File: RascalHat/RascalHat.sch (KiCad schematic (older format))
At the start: 26 parts, among them J10 Conn_01x04_Male, J11 Conn_01x03_Male, J12 Conn_01x03_Male, J13 Conn_01x07_Male, J17 Conn_01x02_Male, J2 Conn_01x09_Male, J3 Conn_01x04_Male, J4 Conn_01x08_Male, J5 Conn_01x08_Male

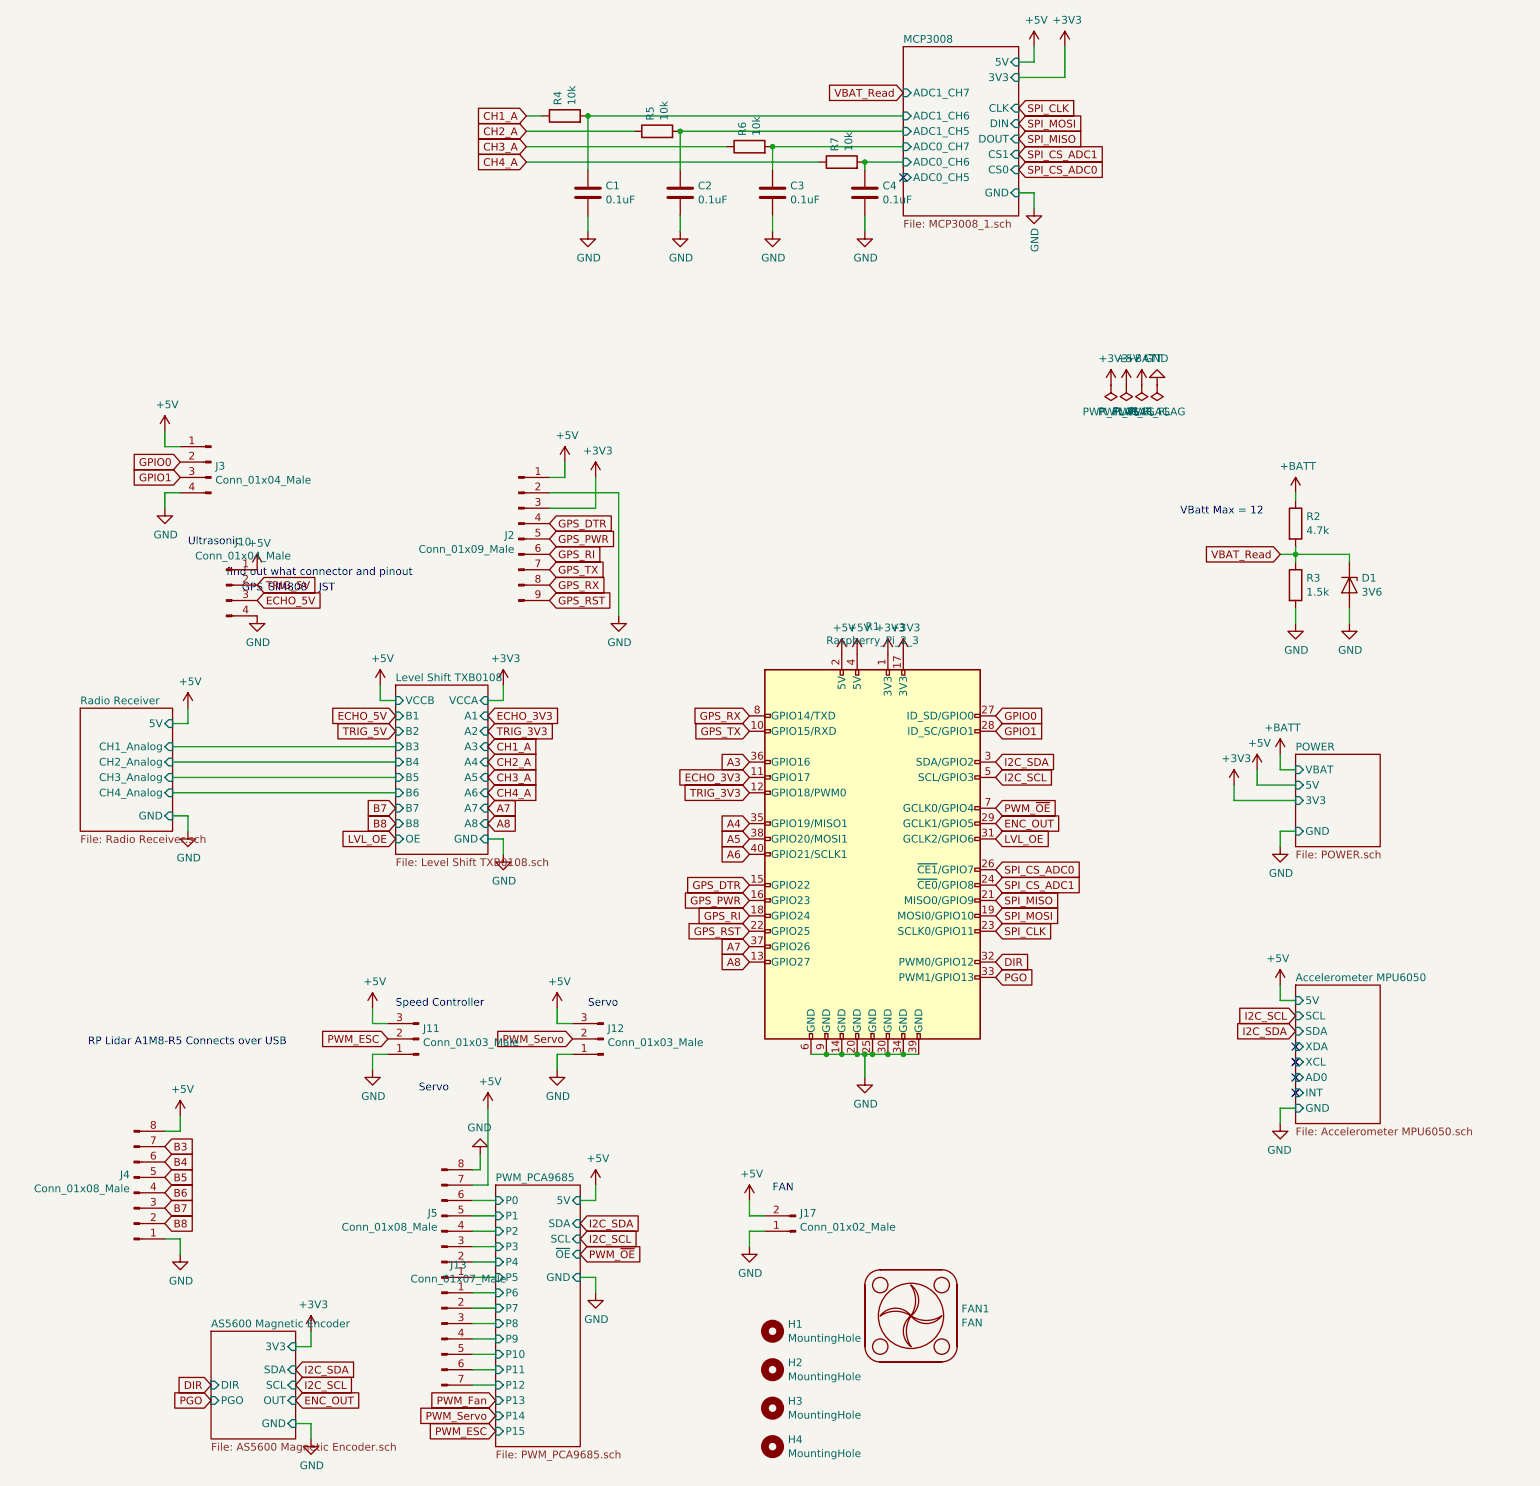
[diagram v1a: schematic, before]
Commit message: schematic updated, all footprints created, pcb layout started
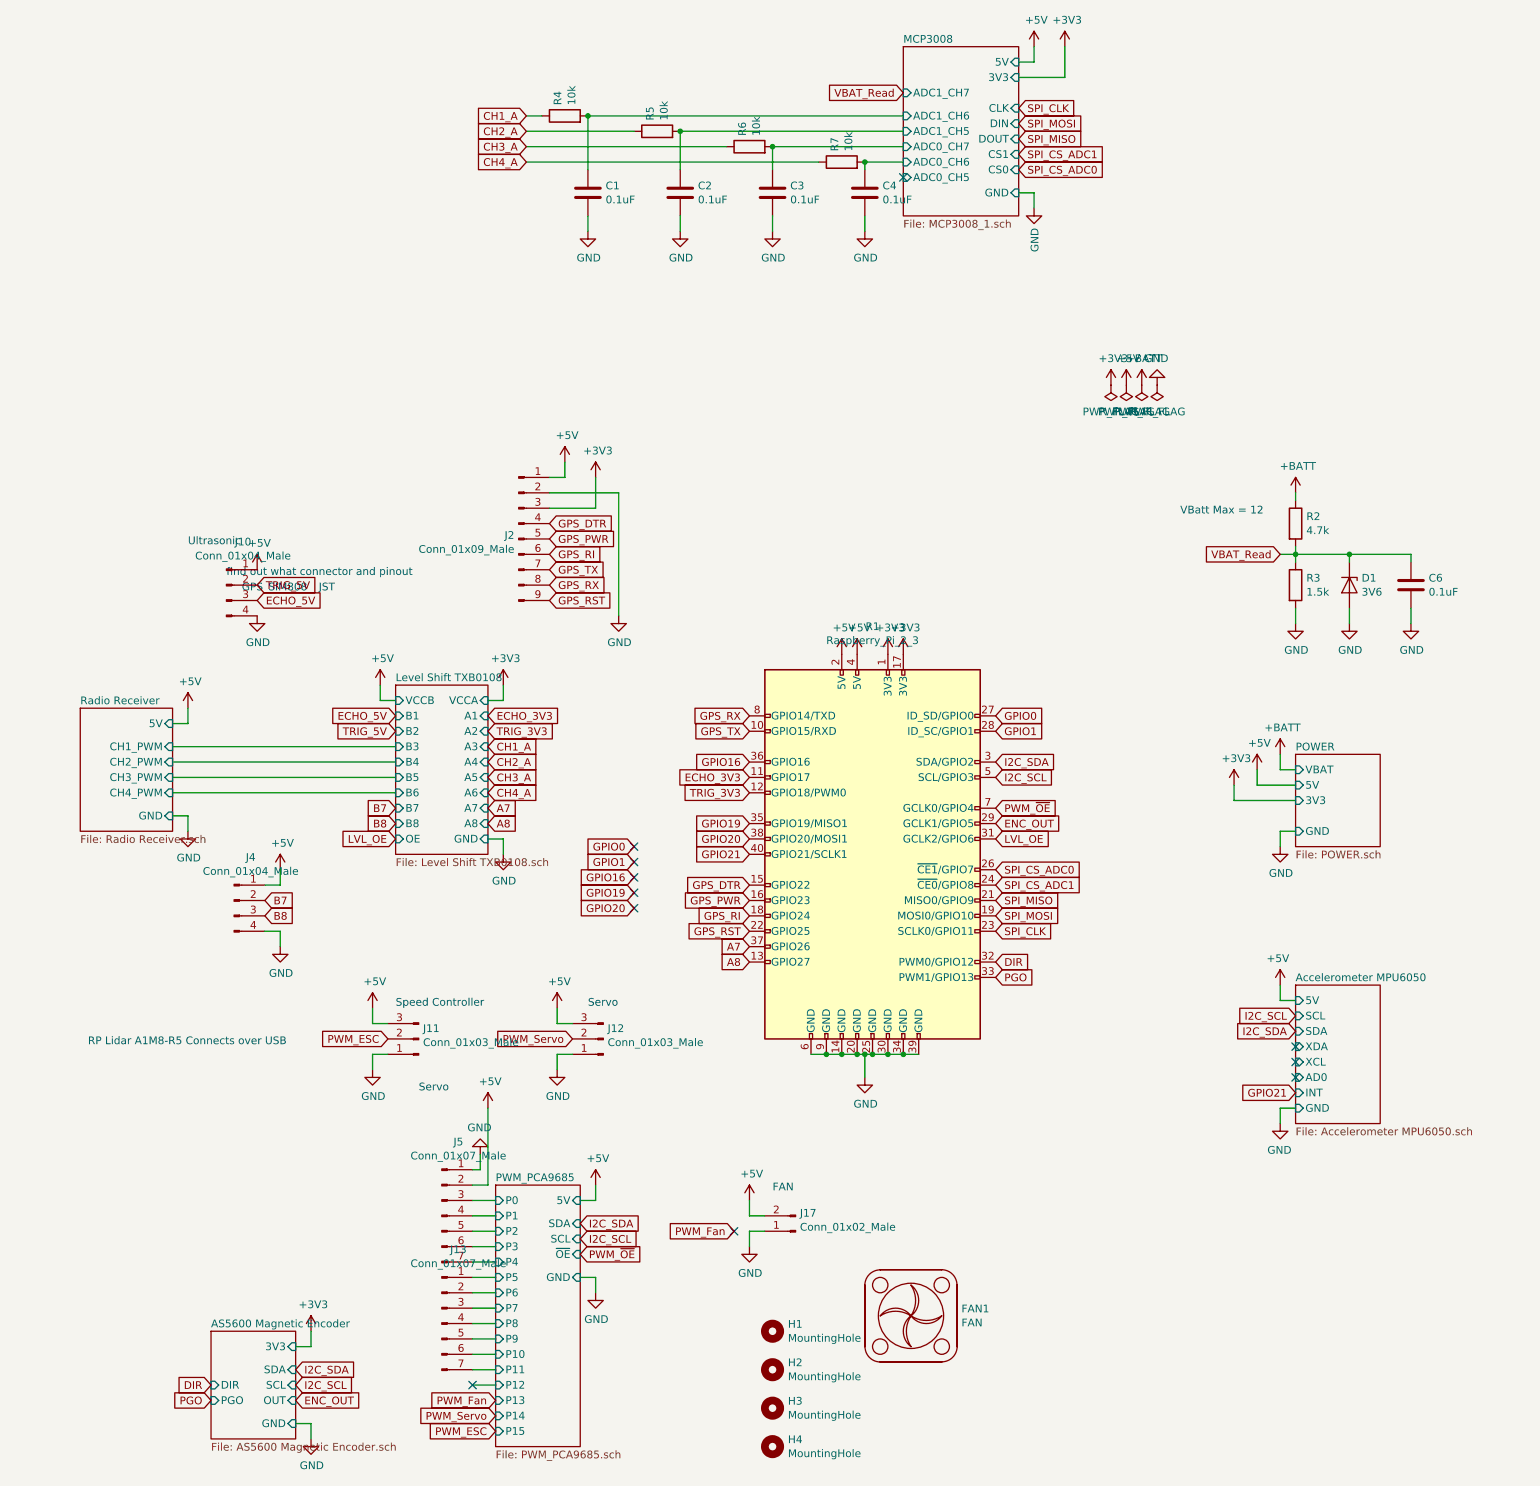
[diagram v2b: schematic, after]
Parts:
- removed J3: Conn_01x04_Male, Connector_JST:JST_EH_B4B-EH-A_1x04_P2.50mm_Vertical, symbol Connector:Conn_01x04_Male
- removed J4, J5: Conn_01x08_Male, Connector_JST:JST_EH_B8B-EH-A_1x08_P2.50mm_Vertical, symbol Connector:Conn_01x08_Male
- added C6: 0.1uF, Capacitor_SMD:C_0805_2012Metric, symbol Device:C
- added J4: Conn_01x04_Male, Connector_JST:JST_EH_B4B-EH-A_1x04_P2.50mm_Vertical, symbol Connector:Conn_01x04_Male
- added J5: Conn_01x07_Male, Connector_JST:JST_EH_B7B-EH-A_1x07_P2.50mm_Vertical, symbol Connector:Conn_01x07_Male
- J2: footprint Connector_JST:JST_EH_B9B-EH-A_1x09_P2.50mm_Vertical -> RascalHat:SIM808-Module
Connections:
- net +5V: now also J4.1 (Pin_1), J5.2 (Pin_2)
- net B7: now also J4.2 (Pin_2)
- net B8: now also J4.3 (Pin_3)
- net GND: now also C6.2, J4.4 (Pin_4), J5.1 (Pin_1)
- net PWM_PCA9685/P0: now also J5.3 (Pin_3)
- net PWM_PCA9685/P1: now also J5.4 (Pin_4)
- net PWM_PCA9685/P10: now also J13.6 (Pin_6); no longer J13.5 (Pin_5)
- net PWM_PCA9685/P11: now also J13.7 (Pin_7); no longer J13.6 (Pin_6)
- net PWM_PCA9685/P12: no longer J13.7 (Pin_7)
- net PWM_PCA9685/P2: now also J5.5 (Pin_5)
- net PWM_PCA9685/P3: now also J5.6 (Pin_6)
- net PWM_PCA9685/P4: now also J5.7 (Pin_7)
- net PWM_PCA9685/P5: now also J13.1 (Pin_1)
- net PWM_PCA9685/P6: now also J13.2 (Pin_2); no longer J13.1 (Pin_1)
- net PWM_PCA9685/P7: now also J13.3 (Pin_3); no longer J13.2 (Pin_2)
- net PWM_PCA9685/P8: now also J13.4 (Pin_4); no longer J13.3 (Pin_3)
- net PWM_PCA9685/P9: now also J13.5 (Pin_5); no longer J13.4 (Pin_4)
- net VBAT_Read: now also C6.1
- net A3 renamed GPIO16
- net A4 renamed GPIO19
- net A5 renamed GPIO20
- net A6 renamed GPIO21
- no-connect marks 5 -> 11
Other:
- moved on the sheet: J13
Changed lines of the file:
@@
 Wire Wire Line
 	5650 5050 5700 5050
-NoConn ~ 8450 5300
 Wire Wire Line
 	3800 6500 3900 6500
@@
 F0 "Radio Receiver" 50
 F1 "Radio Receiver.sch" 50
-F2 "CH1_Analog" I R 1150 3050 50
-F3 "CH2_Analog" I R 1150 3150 50
-F4 "CH3_Analog" I R 1150 3250 50
-F5 "CH4_Analog" I R 1150 3350 50
-F6 "5V" I R 1150 2900 50
-F7 "GND" I R 1150 3500 50
+F2 "5V" I R 1150 2900 50
+F3 "GND" I R 1150 3500 50
+F4 "CH1_PWM" I R 1150 3050 50
+F5 "CH2_PWM" I R 1150 3150 50
+F6 "CH3_PWM" I R 1150 3250 50
+F7 "CH4_PWM" I R 1150 3350 50
 $EndSheet
 Wire Wire Line
@@
 F 0 "J2" H 3372 1724 50  0000 R CNN
 F 1 "Conn_01x09_Male" H 3372 1633 50  0000 R CNN
-F 2 "Connector_JST:JST_EH_B9B-EH-A_1x09_P2.50mm_Vertical" H 3400 1700 50  0001 C CNN
+F 2 "RascalHat:SIM808-Module" H 3400 1700 50  0001 C CNN
 F 3 "~" H 3400 1700 50  0001 C CNN
 	1    3400 1700
@@
 Text GLabel 2600 3550 0    50   Input ~ 0
 B8
-Text GLabel 1100 5650 2    50   Input ~ 0
-B3
-Text GLabel 1100 5750 2    50   Input ~ 0
-B4
-Text GLabel 1100 5850 2    50   Input ~ 0
-B5
-Text GLabel 1100 5950 2    50   Input ~ 0
-B6
-Text GLabel 1100 6050 2    50   Input ~ 0
+Text GLabel 1750 4050 2    50   Input ~ 0
 B7
-Text GLabel 1100 6150 2    50   Input ~ 0
+Text GLabel 1750 4150 2    50   Input ~ 0
 B8
-$Comp
-L Connector:Conn_01x08_Male J4
-U 1 1 6195E622
-P 900 5950
-F 0 "J4" H 872 5832 50  0000 R CNN
-F 1 "Conn_01x08_Male" H 872 5923 50  0000 R CNN
-F 2 "Connector_JST:JST_EH_B8B-EH-A_1x08_P2.50mm_Vertical" H 900 5950 50  0001 C CNN
-F 3 "~" H 900 5950 50  0001 C CNN
-	1    900  5950
-	1    0    0    1
-$EndComp
-Wire Wire Line
-	1100 5550 1200 5550
-Wire Wire Line
-	1200 5550 1200 5450
+Wire Wire Line
+	1750 3950 1850 3950
+Wire Wire Line
+	1850 3950 1850 3850
 $Comp
 L power:+5V #PWR028
 U 1 1 619647F9
-P 1200 5450
-F 0 "#PWR028" H 1200 5300 50  0001 C CNN
-F 1 "+5V" H 1215 5623 50  0000 C CNN
-F 2 "" H 1200 5450 50  0001 C CNN
-F 3 "" H 1200 5450 50  0001 C CNN
-	1    1200 5450
+P 1850 3850
+F 0 "#PWR028" H 1850 3700 50  0001 C CNN
+F 1 "+5V" H 1865 4023 50  0000 C CNN
+F 2 "" H 1850 3850 50  0001 C CNN
+F 3 "" H 1850 3850 50  0001 C CNN
+	1    1850 3850
 	1    0    0    -1
 $EndComp
@@
 L power:GND #PWR043
 U 1 1 6196533F
-P 1200 6350
-F 0 "#PWR043" H 1200 6100 50  0001 C CNN
-F 1 "GND" H 1205 6177 50  0000 C CNN
-F 2 "" H 1200 6350 50  0001 C CNN
-F 3 "" H 1200 6350 50  0001 C CNN
-	1    1200 6350
-	1    0    0    -1
-$EndComp
-Wire Wire Line
-	1200 6350 1200 6250
-Wire Wire Line
-	1200 6250 1100 6250
+P 1850 4350
+F 0 "#PWR043" H 1850 4100 50  0001 C CNN
+F 1 "GND" H 1855 4177 50  0000 C CNN
+F 2 "" H 1850 4350 50  0001 C CNN
+F 3 "" H 1850 4350 50  0001 C CNN
+	1    1850 4350
+	1    0    0    -1
+$EndComp
+Wire Wire Line
+	1850 4350 1850 4250
+Wire Wire Line
+	1850 4250 1750 4250
 Text GLabel 6500 2850 2    50   Input ~ 0
 GPIO0
 Text GLabel 6500 2950 2    50   Input ~ 0
 GPIO1
-Text GLabel 1200 1200 0    50   Input ~ 0
+Text GLabel 4150 3700 0    50   Input ~ 0
 GPIO0
-Text GLabel 1200 1300 0    50   Input ~ 0
+Text GLabel 4150 3800 0    50   Input ~ 0
 GPIO1
 Wire Wire Line
@@
 	1    0    0    -1
 $EndComp
-Wire Wire Line
-	1200 1100 1100 1100
-Wire Wire Line
-	1100 1100 1100 1000
-$Comp
-L power:+5V #PWR04
-U 1 1 61A2CC7D
-P 1100 1000
-F 0 "#PWR04" H 1100 850 50  0001 C CNN
-F 1 "+5V" H 1115 1173 50  0000 C CNN
-F 2 "" H 1100 1000 50  0001 C CNN
-F 3 "" H 1100 1000 50  0001 C CNN
-	1    1100 1000
-	1    0    0    -1
-$EndComp
-$Comp
-L power:GND #PWR07
-U 1 1 61A2D960
-P 1100 1500
-F 0 "#PWR07" H 1100 1250 50  0001 C CNN
-F 1 "GND" H 1105 1327 50  0000 C CNN
-F 2 "" H 1100 1500 50  0001 C CNN
-F 3 "" H 1100 1500 50  0001 C CNN
-	1    1100 1500
-	1    0    0    -1
-$EndComp
-Wire Wire Line
-	1100 1500 1100 1400
-Wire Wire Line
-	1100 1400 1200 1400
 $Sheet
 S 3250 5900 550  1700
@@
 	1    0    0    -1
 $EndComp
-Text GLabel 4900 3150 0    50   Input ~ 0
-A3
-Text GLabel 4900 3550 0    50   Input ~ 0
-A4
-Text GLabel 4900 3650 0    50   Input ~ 0
-A5
-Text GLabel 4900 3750 0    50   Input ~ 0
-A6
 Text GLabel 4900 4350 0    50   Input ~ 0
 A7
@@
 $EndComp
 $Comp
-L Connector:Conn_01x04_Male J3
-U 1 1 61B7022F
-P 1400 1200
-F 0 "J3" H 1372 1174 50  0000 R CNN
-F 1 "Conn_01x04_Male" H 1372 1083 50  0000 R CNN
-F 2 "Connector_JST:JST_EH_B4B-EH-A_1x04_P2.50mm_Vertical" H 1400 1200 50  0001 C CNN
-F 3 "~" H 1400 1200 50  0001 C CNN
-	1    1400 1200
-	-1   0    0    -1
-$EndComp
-$Comp
 L Connector:Conn_01x03_Male J11
 U 1 1 61B7A4C3
@@
 	3450 -850 4750 -850
 $Comp
-L Connector:Conn_01x08_Male J5
-U 1 1 61C838FA
-P 2900 6200
-F 0 "J5" H 2872 6082 50  0000 R CNN
-F 1 "Conn_01x08_Male" H 2872 6173 50  0000 R CNN
-F 2 "Connector_JST:JST_EH_B8B-EH-A_1x08_P2.50mm_Vertical" H 2900 6200 50  0001 C CNN
-F 3 "~" H 2900 6200 50  0001 C CNN
-	1    2900 6200
-	1    0    0    1
-$EndComp
-$Comp
 L Connector:Conn_01x07_Male J?
 U 1 1 61CD4885
-P 2900 6900
+P 2900 6800
 AR Path="/61755993/61CD4885" Ref="J?"  Part="1"
 AR Path="/61CD4885" Ref="J13"  Part="1"
-F 0 "J13" H 3008 7381 50  0000 C CNN
-F 1 "Conn_01x07_Male" H 3008 7290 50  0000 C CNN
-F 2 "Connector_JST:JST_EH_B7B-EH-A_1x07_P2.50mm_Vertical" H 2900 6900 50  0001 C CNN
-F 3 "~" H 2900 6900 50  0001 C CNN
-	1    2900 6900
+F 0 "J13" H 3008 7281 50  0000 C CNN
+F 1 "Conn_01x07_Male" H 3008 7190 50  0000 C CNN
+F 2 "Connector_JST:JST_EH_B7B-EH-A_1x07_P2.50mm_Vertical" H 2900 6800 50  0001 C CNN
+F 3 "~" H 2900 6800 50  0001 C CNN
+	1    2900 6800
 	1    0    0    -1
 $EndComp
@@
 	1    0    0    -1
 $EndComp
+$Comp
+L Connector:Conn_01x04_Male J4
+U 1 1 61D4ADFC
+P 1550 4050
+F 0 "J4" H 1658 4331 50  0000 C CNN
+F 1 "Conn_01x04_Male" H 1658 4240 50  0000 C CNN
+F 2 "Connector_JST:JST_EH_B4B-EH-A_1x04_P2.50mm_Vertical" H 1550 4050 50  0001 C CNN
+F 3 "~" H 1550 4050 50  0001 C CNN
+	1    1550 4050
+	1    0    0    -1
+$EndComp
+$Comp
+L Device:C C6
+U 1 1 61D6F312
+P 9200 2000
+AR Path="/61D6F312" Ref="C6"  Part="1"
+AR Path="/6184E358/61D6F312" Ref="C?"  Part="1"
+F 0 "C6" H 9315 2046 50  0000 L CNN
+F 1 "0.1uF" H 9315 1955 50  0000 L CNN
+F 2 "Capacitor_SMD:C_0805_2012Metric" H 9238 1850 50  0001 C CNN
+F 3 "~" H 9200 2000 50  0001 C CNN
+	1    9200 2000
+	1    0    0    -1
+$EndComp
+Wire Wire Line
+	8800 1800 9200 1800
+Wire Wire Line
+	9200 1800 9200 1850
+Connection ~ 8800 1800
+Wire Wire Line
+	9200 2150 9200 2250
+$Comp
+L power:GND #PWR0116
+U 1 1 61D7A7A3
+P 9200 2250
+F 0 "#PWR0116" H 9200 2000 50  0001 C CNN
+F 1 "GND" H 9205 2077 50  0000 C CNN
+F 2 "" H 9200 2250 50  0001 C CNN
+F 3 "" H 9200 2250 50  0001 C CNN
+	1    9200 2250
+	1    0    0    -1
+$EndComp
+$Comp
+L Connector:Conn_01x07_Male J?
+U 1 1 61D8F3A7
+P 2900 6100
+AR Path="/61755993/61D8F3A7" Ref="J?"  Part="1"
+AR Path="/61D8F3A7" Ref="J5"  Part="1"
+F 0 "J5" H 3008 6581 50  0000 C CNN
+F 1 "Conn_01x07_Male" H 3008 6490 50  0000 C CNN
+F 2 "Connector_JST:JST_EH_B7B-EH-A_1x07_P2.50mm_Vertical" H 2900 6100 50  0001 C CNN
+F 3 "~" H 2900 6100 50  0001 C CNN
+	1    2900 6100
+	1    0    0    -1
+$EndComp
+NoConn ~ 3100 7200
+Text GLabel 4800 6200 0    50   Input ~ 0
+PWM_Fan
+NoConn ~ 4800 6200
+Text GLabel 4900 3150 0    50   Input ~ 0
+GPIO16
+Text GLabel 4900 3550 0    50   Input ~ 0
+GPIO19
+Text GLabel 4900 3650 0    50   Input ~ 0
+GPIO20
+Text GLabel 4900 3750 0    50   Input ~ 0
+GPIO21
+Text GLabel 4150 4000 0    50   Input ~ 0
+GPIO19
+Text GLabel 4150 4100 0    50   Input ~ 0
+GPIO20
+Text GLabel 8450 5300 0    50   Input ~ 0
+GPIO21
+Text GLabel 4150 3900 0    50   Input ~ 0
+GPIO16
+NoConn ~ 4150 3700
+NoConn ~ 4150 3800
+NoConn ~ 4150 3900
+NoConn ~ 4150 4000
+NoConn ~ 4150 4100
 $EndSCHEMATC
